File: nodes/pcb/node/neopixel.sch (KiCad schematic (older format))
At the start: 4 parts, among them U5 WS2811

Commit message: Rearrange
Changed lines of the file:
@@
 AR Path="/5CD1030A/5CCFD4A5" Ref="U7"  Part="1"
 AR Path="/5CD15399/5CCFD4A5" Ref="U8"  Part="1"
-F 0 "U8" V 6600 4350 50  0000 C CNN
+F 0 "U6" V 6600 4350 50  0000 C CNN
 F 1 "WS2811" V 5950 3800 50  0000 C CNN
 F 2 "Package_SO:SSOP-8_3.9x5.05mm_P1.27mm" H 6000 4250 50  0001 C CNN
@@
 AR Path="/5CD1030A/5CCFD4BA" Ref="C11"  Part="1"
 AR Path="/5CD15399/5CCFD4BA" Ref="C12"  Part="1"
-F 0 "C12" H 5050 4200 50  0000 L CNN
+F 0 "C10" H 5050 4200 50  0000 L CNN
 F 1 "0.1uF" H 4950 4000 50  0000 L CNN
 F 2 "Capacitor_SMD:C_0603_1608Metric_Pad1.05x0.95mm_HandSolder" H 5200 4100 50  0001 C CNN
@@
 AR Path="/5CD1030A/5CCFD4E9" Ref="#PWR0147"  Part="1"
 AR Path="/5CD15399/5CCFD4E9" Ref="#PWR0150"  Part="1"
-F 0 "#PWR0150" H 7000 4000 50  0001 C CNN
+F 0 "#PWR0144" H 7000 4000 50  0001 C CNN
 F 1 "GND" H 7005 4077 50  0000 C CNN
 F 2 "" H 7000 4250 50  0001 C CNN
@@
 AR Path="/5CD1030A/5CCFD4F1" Ref="#PWR0148"  Part="1"
 AR Path="/5CD15399/5CCFD4F1" Ref="#PWR0151"  Part="1"
-F 0 "#PWR0151" H 4850 4000 50  0001 C CNN
+F 0 "#PWR0145" H 4850 4000 50  0001 C CNN
 F 1 "GND" H 4855 4077 50  0000 C CNN
 F 2 "" H 4850 4250 50  0001 C CNN
@@
 AR Path="/5CD1030A/5C880ED8" Ref="D3"  Part="1"
 AR Path="/5CD15399/5C880ED8" Ref="D4"  Part="1"
-F 0 "D4" V 6346 2670 50  0000 R CNN
+F 0 "D2" V 6346 2670 50  0000 R CNN
 F 1 "LED_ARGB" V 6255 2670 50  0000 R CNN
 F 2 "LED_SMD:LED_Kingbright_APFA3010_3x1.5mm_Horizontal" H 6300 2950 50  0001 C CNN
@@
 AR Path="/5CD1030A/5C92A31E" Ref="#PWR0146"  Part="1"
 AR Path="/5CD15399/5C92A31E" Ref="#PWR0149"  Part="1"
-F 0 "#PWR0149" H 5450 2050 50  0001 C CNN
+F 0 "#PWR0143" H 5450 2050 50  0001 C CNN
 F 1 "+5V" H 5465 2373 50  0000 C CNN
 F 2 "" H 5450 2200 50  0001 C CNN
@@
 AR Path="/5CD1030A/5CCFD4C2" Ref="R12"  Part="1"
 AR Path="/5CD15399/5CCFD4C2" Ref="R13"  Part="1"
-F 0 "R13" H 5300 3400 50  0000 L CNN
+F 0 "R11" H 5300 3400 50  0000 L CNN
 F 1 "100" H 5300 3150 50  0000 L CNN
 F 2 "Resistor_SMD:R_0603_1608Metric_Pad1.05x0.95mm_HandSolder" V 5490 3290 50  0001 C CNN
@@
 AR Path="/5CD1030A/5C8F192D" Ref="#FLG0103"  Part="1"
 AR Path="/5CD15399/5C8F192D" Ref="#FLG0104"  Part="1"
-F 0 "#FLG0104" H 5750 4075 50  0001 C CNN
+F 0 "#FLG0102" H 5750 4075 50  0001 C CNN
 F 1 "PWR_FLAG" H 5750 4174 50  0000 C CNN
 F 2 "" H 5750 4000 50  0001 C CNN

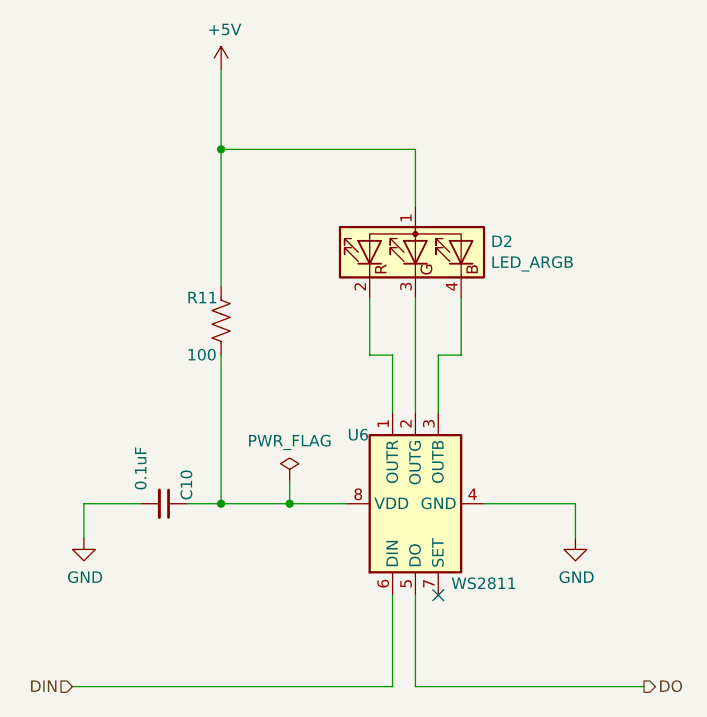
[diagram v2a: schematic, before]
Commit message: Start simplified Seeed OPL compatible circuit
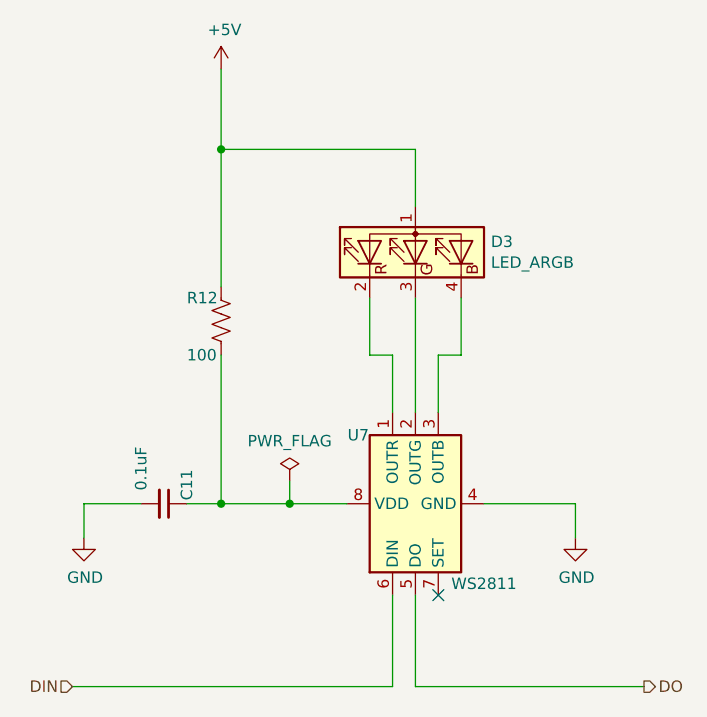
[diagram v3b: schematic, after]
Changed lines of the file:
@@
 EESchema Schematic File Version 4
 LIBS:node-cache
-EELAYER 26 0
+EELAYER 29 0
 EELAYER END
 $Descr A4 11693 8268
 encoding utf-8
-Sheet 3 5
+Sheet 2 3
 Title "NeoPixel Type Circuit"
 Date ""
@@
 AR Path="/5CD1030A/5CCFD4A5" Ref="U7"  Part="1"
 AR Path="/5CD15399/5CCFD4A5" Ref="U8"  Part="1"
-F 0 "U6" V 6600 4350 50  0000 C CNN
+F 0 "U7" V 6600 4350 50  0000 C CNN
 F 1 "WS2811" V 5950 3800 50  0000 C CNN
 F 2 "Package_SO:SSOP-8_3.9x5.05mm_P1.27mm" H 6000 4250 50  0001 C CNN
@@
 AR Path="/5CD1030A/5CCFD4BA" Ref="C11"  Part="1"
 AR Path="/5CD15399/5CCFD4BA" Ref="C12"  Part="1"
-F 0 "C10" H 5050 4200 50  0000 L CNN
+F 0 "C11" H 5050 4200 50  0000 L CNN
 F 1 "0.1uF" H 4950 4000 50  0000 L CNN
 F 2 "Capacitor_SMD:C_0603_1608Metric_Pad1.05x0.95mm_HandSolder" H 5200 4100 50  0001 C CNN
@@
 AR Path="/5CD1030A/5CCFD4E9" Ref="#PWR0147"  Part="1"
 AR Path="/5CD15399/5CCFD4E9" Ref="#PWR0150"  Part="1"
-F 0 "#PWR0144" H 7000 4000 50  0001 C CNN
+F 0 "#PWR0147" H 7000 4000 50  0001 C CNN
 F 1 "GND" H 7005 4077 50  0000 C CNN
 F 2 "" H 7000 4250 50  0001 C CNN
@@
 AR Path="/5CD1030A/5CCFD4F1" Ref="#PWR0148"  Part="1"
 AR Path="/5CD15399/5CCFD4F1" Ref="#PWR0151"  Part="1"
-F 0 "#PWR0145" H 4850 4000 50  0001 C CNN
+F 0 "#PWR0148" H 4850 4000 50  0001 C CNN
 F 1 "GND" H 4855 4077 50  0000 C CNN
 F 2 "" H 4850 4250 50  0001 C CNN
@@
 AR Path="/5CD1030A/5C880ED8" Ref="D3"  Part="1"
 AR Path="/5CD15399/5C880ED8" Ref="D4"  Part="1"
-F 0 "D2" V 6346 2670 50  0000 R CNN
+F 0 "D3" V 6346 2670 50  0000 R CNN
 F 1 "LED_ARGB" V 6255 2670 50  0000 R CNN
 F 2 "LED_SMD:LED_Kingbright_APFA3010_3x1.5mm_Horizontal" H 6300 2950 50  0001 C CNN
@@
 AR Path="/5CD1030A/5C92A31E" Ref="#PWR0146"  Part="1"
 AR Path="/5CD15399/5C92A31E" Ref="#PWR0149"  Part="1"
-F 0 "#PWR0143" H 5450 2050 50  0001 C CNN
+F 0 "#PWR0146" H 5450 2050 50  0001 C CNN
 F 1 "+5V" H 5465 2373 50  0000 C CNN
 F 2 "" H 5450 2200 50  0001 C CNN
@@
 AR Path="/5CD1030A/5CCFD4C2" Ref="R12"  Part="1"
 AR Path="/5CD15399/5CCFD4C2" Ref="R13"  Part="1"
-F 0 "R11" H 5300 3400 50  0000 L CNN
+F 0 "R12" H 5300 3400 50  0000 L CNN
 F 1 "100" H 5300 3150 50  0000 L CNN
 F 2 "Resistor_SMD:R_0603_1608Metric_Pad1.05x0.95mm_HandSolder" V 5490 3290 50  0001 C CNN
@@
 AR Path="/5CD1030A/5C8F192D" Ref="#FLG0103"  Part="1"
 AR Path="/5CD15399/5C8F192D" Ref="#FLG0104"  Part="1"
-F 0 "#FLG0102" H 5750 4075 50  0001 C CNN
+F 0 "#FLG0103" H 5750 4075 50  0001 C CNN
 F 1 "PWR_FLAG" H 5750 4174 50  0000 C CNN
 F 2 "" H 5750 4000 50  0001 C CNN
